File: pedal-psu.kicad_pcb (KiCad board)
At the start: 2 copper layers, 101.6 x 101.6 mm, 65 parts, among them J1 Conn_01x01_Male, J2 Conn_01x01_Male, J3 Conn_01x02_Male, J4 Conn_01x02_Male, J5 Conn_01x02_Male, J6 Conn_01x02_Male, T1 Transformer_1P_1S, T2 Transformer_1P_1S, U1 LM7809_TO220, U2 LM324, U4 LM7805_TO220, U5 LM317_3PinPackage

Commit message: Complete schematic, moving on to PCB design.
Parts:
- removed J5, J6: Conn_01x02_Male, Connector_Molex:Molex_KK-254_AE-6410-02A_1x02_P2.54mm_Vertical
- added C15: 100n, Capacitor_SMD:C_1210_3225Metric_Pad1.42x2.65mm_HandSolder, F.Cu at (266.8, 91.8)
- added C16: CP, Capacitor_THT:C_Radial_D10.0mm_H12.5mm_P5.00mm, F.Cu at (233.9, 95.4)
- added C17: CP, Capacitor_THT:C_Radial_D6.3mm_H5.0mm_P2.50mm, F.Cu at (244.9, 108.7)
- added C18: CP, Capacitor_THT:C_Radial_D6.3mm_H5.0mm_P2.50mm, F.Cu at (254.9, 99.6)
- added C19: 100n, Capacitor_SMD:C_1210_3225Metric_Pad1.42x2.65mm_HandSolder, F.Cu at (253.0, 106.8)
- added C20: 100n, Capacitor_SMD:C_1210_3225Metric_Pad1.42x2.65mm_HandSolder, F.Cu at (263.1, 96.3)
- added D10: 1N4001, Diode_SMD:D_SMA_Handsoldering, F.Cu at (247.2, 97.9)
- added D11: 1N4001, Diode_SMD:D_SMA_Handsoldering, F.Cu at (258.8, 91.9)
- added D12: 1N4001, Diode_SMD:D_SMA_Handsoldering, F.Cu at (247.2, 102.5)
- added D9: 1N4001, Diode_SMD:D_SMA_Handsoldering, F.Cu at (235.7, 109.5)
- added J7: Status LEDS, Connector_Molex:Molex_KK-254_AE-6410-10A_1x10_P2.54mm_Vertical, F.Cu at (306.1, 163.8)
- added R26: 220, Resistor_SMD:R_0805_2012Metric_Pad1.15x1.40mm_HandSolder, F.Cu at (240.0, 66.0)
- added R30: 100k, Resistor_SMD:R_0805_2012Metric_Pad1.15x1.40mm_HandSolder, F.Cu at (275.6, 145.8)
- added R31: 560, Resistor_SMD:R_0805_2012Metric_Pad1.15x1.40mm_HandSolder, F.Cu at (299.5, 161.3)
- added R32: 560, Resistor_SMD:R_0805_2012Metric_Pad1.15x1.40mm_HandSolder, F.Cu at (299.5, 158.8)
- added R33: 560, Resistor_SMD:R_0805_2012Metric_Pad1.15x1.40mm_HandSolder, F.Cu at (299.5, 156.2)
- added R34: 560, Resistor_SMD:R_0805_2012Metric_Pad1.15x1.40mm_HandSolder, F.Cu at (299.5, 153.7)
- added R35: 560, Resistor_SMD:R_0805_2012Metric_Pad1.15x1.40mm_HandSolder, F.Cu at (299.5, 151.1)
- added R36: 560, Resistor_SMD:R_0805_2012Metric_Pad1.15x1.40mm_HandSolder, F.Cu at (299.5, 148.6)
- added R37: 560, Resistor_SMD:R_0805_2012Metric_Pad1.15x1.40mm_HandSolder, F.Cu at (299.5, 146.1)
- added R38: 560, Resistor_SMD:R_0805_2012Metric_Pad1.15x1.40mm_HandSolder, F.Cu at (299.5, 143.5)
- added RV4: 10k, Potentiometer_THT:Potentiometer_Piher_PT-6-V_Vertical, F.Cu at (222.2, 57.1)
- added U3: LM7809_TO220, Package_TO_SOT_THT:TO-220-3_Vertical, F.Cu at (233.9, 105.1)
- added U6: LM7809_TO220, Package_TO_SOT_THT:TO-220-3_Vertical, F.Cu at (245.4, 93.6)
- added U7: 74HC595, Package_SO:SOP-16_4.4x10.4mm_P1.27mm, F.Cu at (288.9, 150.5)
- C12, D4, D6, R19, R25: moved to B.Cu
- J3: value Conn_01x02_Male -> Power Sockets; footprint Connector_Molex:Molex_KK-254_AE-6410-02A_1x02_P2.54mm_Vertical -> Connector_Molex:Molex_KK-254_AE-6410-10A_1x10_P2.54mm_Vertical
- J4: value Conn_01x02_Male -> LCD Display; footprint Connector_Molex:Molex_KK-254_AE-6410-02A_1x02_P2.54mm_Vertical -> Connector_Molex:Molex_KK-254_AE-6410-10A_1x10_P2.54mm_Vertical
- T1, T2: footprint Transformer_THT:Transformer_CHK_EI42-5VA_1xSec -> pedal-psu:Transformer_V42AJ
- moved A1 117.3 mm to (182.9, 158.8)
- moved R19 111.7 mm to (106.7, 142.2)
- moved C9 96.1 mm to (102.8, 109.2), turned to 180 degrees
- moved J3 94.6 mm to (121.9, 172.7)
- moved F2 87.8 mm to (113.0, 54.6)
- moved R25 86.8 mm to (104.1, 148.6), turned to 270 degrees
- moved RV2 85.3 mm to (105.4, 55.9), turned to 180 degrees
- moved D1 82.0 mm to (171.4, 99.1), turned to 180 degrees
- moved F1 80.0 mm to (161.3, 54.6)
- moved RV1 79.9 mm to (153.7, 55.9), turned to 180 degrees
- moved C14 68.3 mm to (100.3, 125.7)
- moved D6 66.6 mm to (97.8, 130.8), turned to 180 degrees
- moved D4 62.9 mm to (102.8, 135.9), turned to 180 degrees
- moved C12 60.1 mm to (96.5, 147.3)
- moved RV3 50.6 mm to (95.2, 142.2)
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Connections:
- net Net-(A1-Pad15) renamed MISO
- A1 pad 10: Net-(A1-Pad10) -> LCD7
- A1 pad 11: Net-(A1-Pad11) -> RS
- A1 pad 12: Net-(A1-Pad12) -> ENABLE
- A1 pad 13: Net-(A1-Pad13) -> SS
- A1 pad 14: Net-(A1-Pad14) -> MOSI
- A1 pad 16: Net-(A1-Pad16) -> SCK
- A1 pad 5: Net-(A1-Pad5) -> BUTTON
- A1 pad 7: Net-(A1-Pad7) -> LCD4
- A1 pad 8: Net-(A1-Pad8) -> LCD5
- A1 pad 9: Net-(A1-Pad9) -> LCD6
- C10 pad 2: Net-(C10-Pad2) -> GND
- C11 pad 2: Net-(C11-Pad2) -> GND
- C12 pad 2: Net-(C10-Pad2) -> GND
- C13 pad 2: Net-(C11-Pad2) -> GND
- C14 pad 2: Net-(C10-Pad2) -> GND
- C3 pad 1: +9V -> +9V_1
- C4 pad 1: +9V -> +9V_1
- C9 pad 2: Net-(C10-Pad2) -> GND
- D5 pad 2: +9V -> +9V_1
- D7 pad 1: +9V -> +9V_1
- D8 pad 2: Net-(C11-Pad2) -> GND
- J3 pad 1: +9V -> GND
- J3 pad 2: Net-(J3-Pad2) -> +9V_1
- J4 pad 1: +9V -> GND
- J4 pad 2: Net-(J4-Pad2) -> +5V
- R1 pad 1: +9V -> +9V_1
- R21 pad 1: Net-(J6-Pad2) -> GND_ADJ
- R3 pad 1: +9V -> +9V_2
- R5 pad 1: +9V -> +9V_3
- R7 pad 1: Net-(J3-Pad2) -> GND_1
- R8 pad 1: Net-(J4-Pad2) -> GND_2
- R9 pad 1: Net-(J5-Pad2) -> GND_3
- RV3 pad 2: Net-(C10-Pad2) -> GND
- RV3 pad 3: Net-(C10-Pad2) -> GND
- U1 pad 3: +9V -> +9V_1
- U2 pad 10: Net-(J5-Pad2) -> GND_3
- U2 pad 12: Net-(J6-Pad2) -> GND_ADJ
- U2 pad 3: Net-(J3-Pad2) -> GND_1
- U2 pad 5: Net-(J4-Pad2) -> GND_2
- U4 pad 2: Net-(C11-Pad2) -> GND
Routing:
- net Net-(J2-Pad1): track 0.00 -> 140.1 mm
- net Net-(F1-Pad2): track 0.00 -> 69.8 mm
- net Net-(F1-Pad1): track 0.00 -> 27.0 mm
- net Net-(F2-Pad1): track 0.00 -> 26.4 mm
- net Net-(C10-Pad1): track 0.00 -> 22.1 mm
- net Net-(C12-Pad1): track 0.00 -> 18.6 mm
- net Net-(R31-Pad1): track 0.00 -> 15.9 mm
- net +ADJV: track 0.00 -> 10.2 mm
- net Net-(R38-Pad1): track 0.00 -> 7.98 mm
- net Net-(R32-Pad1): track 0.00 -> 7.97 mm
- net Net-(R33-Pad1): track 0.00 -> 7.45 mm
- net Net-(R37-Pad1): track 0.00 -> 7.45 mm
- net Net-(R34-Pad1): track 0.00 -> 6.93 mm
- net Net-(R36-Pad1): track 0.00 -> 6.93 mm
- net Net-(R35-Pad1): track 0.00 -> 6.40 mm
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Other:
- board size 101.6 x 101.6 mm -> 139.7 x 101.6 mm
- net class Default: clearance 0.2 -> 0.4; trace_width 0.25 -> 0.6; via_dia 0.8 -> 1; via_drill 0.4 -> 0.5
- rule trace_clearance: 0.2 -> 0.4

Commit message: Moved things around on PCB
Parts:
- C19, C20, C4, D10, D11, D12, D5, D7, D9: moved to B.Cu
- moved C13 158.1 mm to (299.1, 35.8)
- moved J4 158.1 mm to (284.5, 62.2)
- moved R10 158.1 mm to (317.0, 23.1)
- moved R24 158.1 mm to (317.0, 20.2)
- moved R6 158.1 mm to (321.7, 18.6)
- moved A1 158.1 mm to (306.1, 59.7)
- moved C5 158.1 mm to (311.6, 23.0)
- moved C7 158.1 mm to (302.6, 30.9)
- moved C8 158.1 mm to (285.4, 43.6)
- moved R11 158.1 mm to (298.5, 39.3)
- moved R12 158.1 mm to (304.4, 34.5)
- moved R13 158.1 mm to (296.7, 43.0)
- moved R15 158.1 mm to (316.7, 17.2)
- moved R17 158.1 mm to (323.9, 15.6)
- moved R23 158.1 mm to (307.9, 30.2)
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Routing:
- net Net-(F2-Pad1): track 26.4 -> 27.0 mm
- net Net-(F1-Pad1): track 27.0 -> 26.4 mm

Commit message: Moving Op-Amp into place.
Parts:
- added C21: 100n, Capacitor_SMD:C_1210_3225Metric_Pad1.42x2.65mm_HandSolder, B.Cu at (163.4, 120.1)
- C12: value C -> 100n
- C13: value C -> 100n; moved to B.Cu
- C6, D3, D8, R20, R21, R7, R8, R9: moved to B.Cu
- D1, D2: footprint Diode_THT:Diode_Bridge_Vishay_KBL -> PartsStash:Diode_Bridge_TELPOD_GB009_p4mm
- F1, F2: footprint pedal-psu:Fuse-PTF15 -> PartsStash:Fuse-PTF15
- J1, J2: footprint pedal-psu:Blade_3866B.68 -> PartsStash:Blade_3866B.68
- T1, T2: footprint pedal-psu:Transformer_V42AJ -> PartsStash:Transformer_V42AJ
- U1, U3, U4, U5, U6: footprint Package_TO_SOT_THT:TO-220-3_Vertical -> PartsStash:TO220_Vertical_Radiator_L15mm_W10mm
- moved R17 233.2 mm to (121.4, 131.3), turned to 180 degrees
- moved R10 228.6 mm to (114.3, 128.8)
- moved R8 220.1 mm to (108.5, 137.0), turned to 90 degrees
- moved R7 208.5 mm to (103.4, 137.0), turned to 90 degrees
- moved R13 204.5 mm to (112.3, 131.3)
- moved R11 203.2 mm to (117.3, 131.3), turned to 180 degrees
- moved R21 192.8 mm to (118.6, 137.0), turned to 90 degrees
- moved R14 179.9 mm to (119.4, 128.8), turned to 180 degrees
- moved C8 176.2 mm to (163.4, 170.7), turned to 180 degrees
- moved C13 144.5 mm to (181.6, 119.9), turned to 180 degrees
- moved R16 134.5 mm to (110.2, 128.8)
- moved U2 108.2 mm to (115.8, 137.9), turned to 270 degrees
- moved R15 105.7 mm to (237.5, 87.1)
- moved R23 101.6 mm to (240.0, 105.8)
- moved R24 101.6 mm to (249.0, 95.8)
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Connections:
- T1 pad 3: Net-(D1-Pad3) -> Net-(D1-Pad2)
- T1 pad 4: Net-(D1-Pad2) -> Net-(D1-Pad3)
- U2 pad 1: Net-(R13-Pad1) -> Net-(R14-Pad1)
- U2 pad 2: Net-(R10-Pad1) -> Net-(R11-Pad1)
- U2 pad 3: GND_1 -> GND_2
- U2 pad 5: GND_2 -> GND_1
- U2 pad 6: Net-(R11-Pad1) -> Net-(R10-Pad1)
- U2 pad 7: Net-(R14-Pad1) -> Net-(R13-Pad1)
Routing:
- net Net-(C1-Pad1): track 0.00 -> 87.7 mm
- net +9V_3: track 0.00 -> 79.0 mm
- net +ADJV: track 10.2 -> 84.2 mm
- net +9V_2: track 0.00 -> 67.0 mm
- net Net-(C10-Pad1): track 22.1 -> 80.4 mm
- net +9V_1: track 0.00 -> 57.2 mm
- net Net-(D2-Pad3): track 0.00 -> 33.5 mm
- net Net-(D1-Pad3): track 0.00 -> 32.2 mm
- net +5V: track 0.00 -> 32.0 mm
- net GND_1: track 0.00 -> 27.0 mm, vias 0 -> 1
- net GND_2: track 0.00 -> 26.4 mm, vias 0 -> 1
- net Net-(D2-Pad2): track 0.00 -> 21.8 mm
- net Net-(D1-Pad2): track 0.00 -> 20.5 mm
- net GND_3: track 0.00 -> 14.9 mm, vias 0 -> 1
- net GND_ADJ: track 0.00 -> 14.6 mm, vias 0 -> 1
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
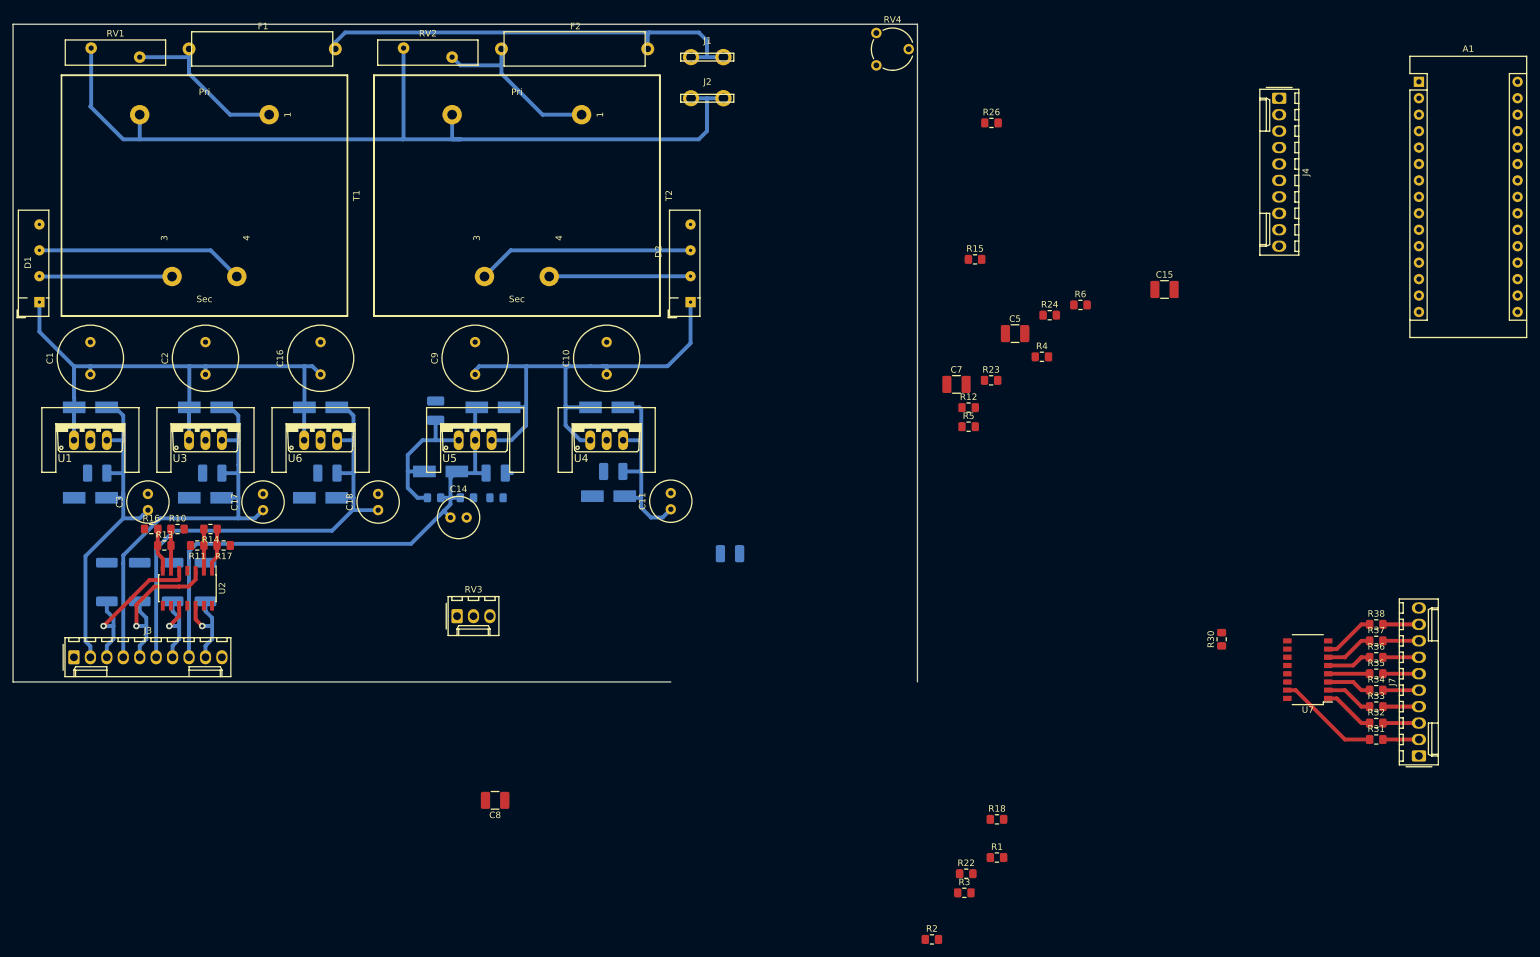
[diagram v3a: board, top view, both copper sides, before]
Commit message: Complete PCB ready for hand etching.
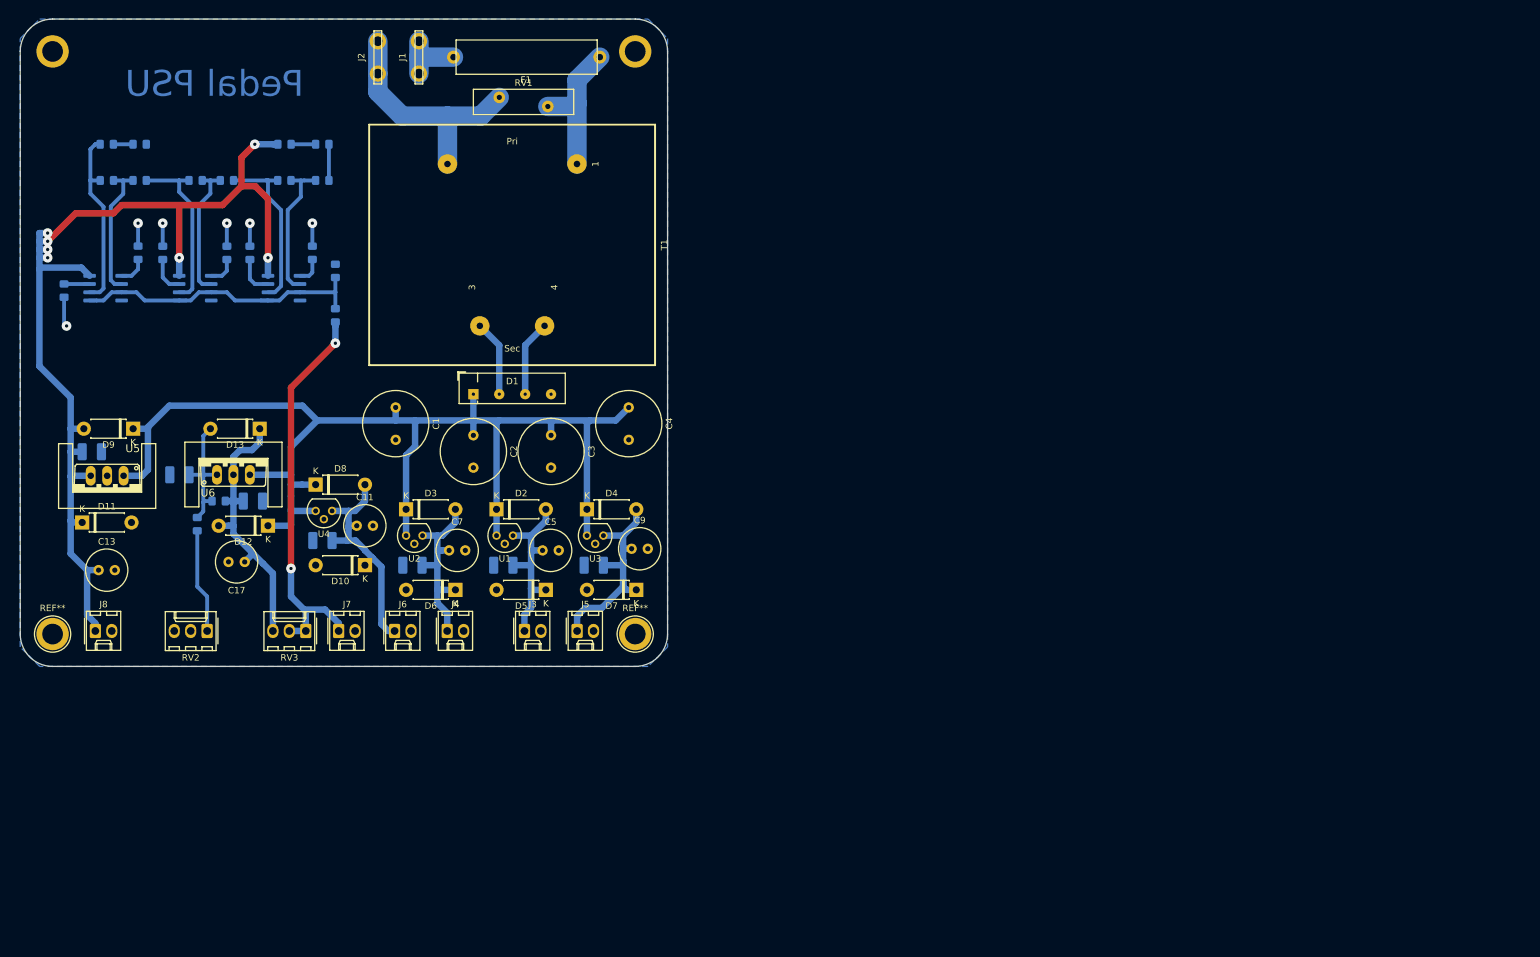
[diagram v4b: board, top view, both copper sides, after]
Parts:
- removed A1: Arduino_Nano_v3.x, Module:Arduino_Nano
- removed C18: CP, Capacitor_THT:C_Radial_D6.3mm_H5.0mm_P2.50mm
- removed C19, C20, C21: 100n, Capacitor_SMD:C_1210_3225Metric_Pad1.42x2.65mm_HandSolder
- removed F2: Fuse, PartsStash:Fuse-PTF15
- removed R21: R1, Resistor_SMD:R_2512_6332Metric_Pad1.52x3.35mm_HandSolder
- removed R22, R24: 1k, Resistor_SMD:R_0805_2012Metric_Pad1.15x1.40mm_HandSolder
- removed R23: 20k, Resistor_SMD:R_0805_2012Metric_Pad1.15x1.40mm_HandSolder
- removed R25: R, Resistor_SMD:R_0805_2012Metric_Pad1.15x1.40mm_HandSolder
- removed R26: 220, Resistor_SMD:R_0805_2012Metric_Pad1.15x1.40mm_HandSolder
- removed R30: 100k, Resistor_SMD:R_0805_2012Metric_Pad1.15x1.40mm_HandSolder
- removed R31, R32, R33, R34, R35, R36, R37, R38: 560, Resistor_SMD:R_0805_2012Metric_Pad1.15x1.40mm_HandSolder
- removed RV4: 10k, Potentiometer_THT:Potentiometer_Piher_PT-6-V_Vertical
- removed T2: Transformer_1P_1S, PartsStash:Transformer_V42AJ
- added ?: , , F.Cu at (0.00, -90.0)
- added ?: , , F.Cu at (-90.0, -90.0)
- added D13: 1N4001, Diode_THT:D_DO-41_SOD81_P7.62mm_Horizontal, F.Cu at (127.0, 113.3)
- added J5: Conn_01x02_Male, Connector_Molex:Molex_KK-254_AE-6410-02A_1x02_P2.54mm_Vertical, F.Cu at (176.0, 144.5)
- added J6: Conn_01x02_Male, Connector_Molex:Molex_KK-254_AE-6410-02A_1x02_P2.54mm_Vertical, F.Cu at (147.8, 144.5)
- added J8: Conn_01x02_Male, Connector_Molex:Molex_KK-254_AE-6410-02A_1x02_P2.54mm_Vertical, F.Cu at (101.6, 144.5)
- added REF**: Banana_Jack_1Pin, Connector:Banana_Jack_1Pin, F.Cu at (95.0, 145.0)
- added REF**: Banana_Jack_1Pin, Connector:Banana_Jack_1Pin, F.Cu at (185.0, 145.0)
- added U8: LM358, Package_SO:SOIC-8_3.9x4.9mm_P1.27mm, B.Cu at (117.0, 91.6)
- added U9: LM358, Package_SO:SOIC-8_3.9x4.9mm_P1.27mm, B.Cu at (130.7, 91.6)
- C10, C16: value CP -> 100n; footprint Capacitor_THT:C_Radial_D10.0mm_H12.5mm_P5.00mm -> Capacitor_SMD:C_1210_3225Metric_Pad1.42x2.65mm_HandSolder; moved to B.Cu
- C13: value 100n -> CP; footprint Capacitor_SMD:C_1210_3225Metric_Pad1.42x2.65mm_HandSolder -> Capacitor_THT:C_Radial_D6.3mm_H5.0mm_P2.50mm; moved to F.Cu
- C14: value CP -> 100n; footprint Capacitor_THT:C_Radial_D6.3mm_H5.0mm_P2.50mm -> Capacitor_SMD:C_1210_3225Metric_Pad1.42x2.65mm_HandSolder; moved to B.Cu
- C15, C8, R10, R11, R12: moved to B.Cu
- C3: footprint Capacitor_THT:C_Radial_D6.3mm_H5.0mm_P2.50mm -> Capacitor_THT:C_Radial_D10.0mm_H12.5mm_P5.00mm
- C4: value 100n -> CP; footprint Capacitor_SMD:C_1210_3225Metric_Pad1.42x2.65mm_HandSolder -> Capacitor_THT:C_Radial_D10.0mm_H12.5mm_P5.00mm; moved to F.Cu
- C5, C7: value 100n -> CP; footprint Capacitor_SMD:C_1210_3225Metric_Pad1.42x2.65mm_HandSolder -> Capacitor_THT:C_Radial_D6.3mm_H5.0mm_P2.50mm
- C9: footprint Capacitor_THT:C_Radial_D10.0mm_H12.5mm_P5.00mm -> Capacitor_THT:C_Radial_D6.3mm_H5.0mm_P2.50mm
- D10, D11, D12, D3, D4, D5, D6, D7, D8, D9: footprint Diode_SMD:D_SMA_Handsoldering -> Diode_THT:D_DO-41_SOD81_P7.62mm_Horizontal; moved to F.Cu
- D2: value D_Bridge_+AA- -> 1N4001; footprint PartsStash:Diode_Bridge_TELPOD_GB009_p4mm -> Diode_THT:D_DO-41_SOD81_P7.62mm_Horizontal
- J3: value Power Sockets -> Conn_01x02_Male; footprint Connector_Molex:Molex_KK-254_AE-6410-10A_1x10_P2.54mm_Vertical -> Connector_Molex:Molex_KK-254_AE-6410-02A_1x02_P2.54mm_Vertical
- J4: value LCD Display -> Conn_01x02_Male; footprint Connector_Molex:Molex_KK-254_AE-6410-10A_1x10_P2.54mm_Vertical -> Connector_Molex:Molex_KK-254_AE-6410-02A_1x02_P2.54mm_Vertical
- J7: value Status LEDS -> Conn_01x02_Male; footprint Connector_Molex:Molex_KK-254_AE-6410-10A_1x10_P2.54mm_Vertical -> Connector_Molex:Molex_KK-254_AE-6410-02A_1x02_P2.54mm_Vertical
- R1: value 10k -> 270; moved to B.Cu
- R13: value 20k -> 3k9; moved to B.Cu
- R14: value 20k -> 100R; moved to B.Cu
- R15: value 20k -> 470R; moved to B.Cu
- R16, R17, R18: value 1k -> 470R; moved to B.Cu
- R19: value 10k -> 470R
- R2: value 2k2 -> 470; moved to B.Cu
- R20: value 2k2 -> 470R
- R3: value 10k -> 22k; moved to B.Cu
- R4: value 2k2 -> 22k; moved to B.Cu
- R5: value 10k -> 3k9; moved to B.Cu
- R6: value 2k2 -> 3k9; moved to B.Cu
- R7: value R1 -> 1k2; footprint Resistor_SMD:R_2512_6332Metric_Pad1.52x3.35mm_HandSolder -> Resistor_SMD:R_0805_2012Metric_Pad1.15x1.40mm_HandSolder
- R8, R9: value R1 -> 1k; footprint Resistor_SMD:R_2512_6332Metric_Pad1.52x3.35mm_HandSolder -> Resistor_SMD:R_0805_2012Metric_Pad1.15x1.40mm_HandSolder
- RV2: value Varistor -> 1K; footprint Varistor:RV_Disc_D15.5mm_W3.9mm_P7.5mm -> Connector_Molex:Molex_KK-254_AE-6410-03A_1x03_P2.54mm_Vertical
- RV3: value 100k -> 2K
- U1, U3: value LM7809_TO220 -> LM78L09; footprint PartsStash:TO220_Vertical_Radiator_L15mm_W10mm -> Package_TO_SOT_THT:TO-92
- U2: value LM324 -> LM78L09; footprint Package_SO:SOIC-14_3.9x8.7mm_P1.27mm -> Package_TO_SOT_THT:TO-92
- U4: value LM7805_TO220 -> LM78L09; footprint PartsStash:TO220_Vertical_Radiator_L15mm_W10mm -> Package_TO_SOT_THT:TO-92
- U5: value LM317_3PinPackage -> LM7809_TO220
- U6: value LM7809_TO220 -> LM317_3PinPackage
- U7: value 74HC595 -> LM358; footprint Package_SO:SOP-16_4.4x10.4mm_P1.27mm -> Package_SO:SOIC-8_3.9x4.9mm_P1.27mm; moved to B.Cu
- moved U7 194.8 mm to (103.2, 91.6)
- moved J7 168.0 mm to (139.2, 144.5), turned to 0 degrees
- moved C15 154.8 mm to (114.6, 120.4), turned to 180 degrees
- moved J4 152.6 mm to (156.0, 144.5), turned to 0 degrees
- moved R18 147.7 mm to (121.9, 86.1), turned to 90 degrees
- moved R12 137.7 mm to (103.4, 74.9), turned to 180 degrees
- moved R1 132.2 mm to (120.7, 124.5), turned to 180 degrees
- moved R3 131.9 mm to (138.7, 95.8), turned to 90 degrees
- moved R2 130.4 mm to (117.3, 128.0), turned to 270 degrees
- moved R6 119.7 mm to (136.7, 69.3)
- moved R5 114.3 mm to (130.8, 69.3)
- moved R15 112.0 mm to (125.5, 86.1), turned to 90 degrees
- moved R4 109.9 mm to (138.7, 88.9), turned to 90 degrees
- moved RV2 96.4 mm to (118.9, 144.5)
- moved D7 85.5 mm to (185.2, 138.2)
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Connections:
- net VS3 renamed Net-(R5-Pad2)
- C1 pad 1: Net-(C1-Pad1) -> +12V
- C10 pad 1: Net-(C10-Pad1) -> +9V_2
- C11 pad 1: +5V -> +9V_1
- C12 pad 1: Net-(C12-Pad1) -> +9V_1
- C13 pad 1: +5V -> +9V_5
- C14 pad 1: +ADJV -> +9V_5
- C15 pad 1: +5V -> Net-(C15-Pad1)
- C16 pad 1: Net-(C1-Pad1) -> /ADJ
- C17 pad 1: +9V_2 -> /ADJ
- C2 pad 1: Net-(C1-Pad1) -> +12V
- C3 pad 1: +9V_1 -> +12V
- C4 pad 1: +9V_1 -> +12V
- C5 pad 1: IS1 -> +9V_3
- C6 pad 1: IS2 -> +9V_3
- C7 pad 1: IS3 -> +9V_4
- C8 pad 1: IS4 -> +9V_4
- C9 pad 1: Net-(C10-Pad1) -> +9V_2
- D1 pad 1: Net-(C1-Pad1) -> +12V
- D10 pad 1: Net-(C1-Pad1) -> +9V_1
- D10 pad 2: +9V_3 -> GND
- D11 pad 1: +9V_2 -> +9V_5
- D12 pad 1: +9V_3 -> +12V
- D12 pad 2: GND -> /ADJ
- D2 pad 1: Net-(C10-Pad1) -> +12V
- D2 pad 2: Net-(D2-Pad2) -> +9V_3
- D3 pad 1: Net-(C10-Pad1) -> +12V
- D3 pad 2: +5V -> +9V_4
- D4 pad 1: Net-(C10-Pad1) -> +12V
- D4 pad 2: +ADJV -> +9V_2
- D5 pad 1: Net-(C1-Pad1) -> +9V_3
- D5 pad 2: +9V_1 -> GND
- D6 pad 1: +ADJV -> +9V_4
- D6 pad 2: Net-(C12-Pad1) -> GND
- D7 pad 1: +9V_1 -> +9V_2
- D8 pad 1: +5V -> +12V
- D8 pad 2: GND -> +9V_1
- D9 pad 1: Net-(C1-Pad1) -> +12V
- D9 pad 2: +9V_2 -> +9V_5
- J3 pad 1: GND -> +9V_3
- J3 pad 2: +9V_1 -> GND
- J4 pad 1: GND -> +9V_4
- J4 pad 2: +5V -> GND
- J7 pad 1: GND -> +ADJV
- J7 pad 2: Net-(J7-Pad2) -> GND
- R1 pad 1: +9V_1 -> /ADJ
- R1 pad 2: VS1 -> Net-(C15-Pad1)
- R10 pad 2: GND -> Net-(R10-Pad2)
- R11 pad 1: Net-(R11-Pad1) -> Net-(R10-Pad2)
- R11 pad 2: GND -> Net-(R11-Pad2)
- R12 pad 1: Net-(R12-Pad1) -> Net-(R11-Pad2)
- R12 pad 2: GND -> Net-(R12-Pad2)
- R13 pad 1: Net-(R13-Pad1) -> Net-(R12-Pad2)
- R13 pad 2: Net-(R10-Pad1) -> Net-(R13-Pad2)
- R14 pad 1: Net-(R14-Pad1) -> Net-(R13-Pad2)
- R14 pad 2: Net-(R11-Pad1) -> GND
- R15 pad 2: Net-(R12-Pad1) -> Net-(R15-Pad2)
- R16 pad 1: IS1 -> Net-(R16-Pad1)
- R16 pad 2: Net-(R13-Pad1) -> Net-(R16-Pad2)
- R17 pad 1: IS2 -> Net-(R17-Pad1)
- R17 pad 2: Net-(R14-Pad1) -> Net-(R17-Pad2)
- R18 pad 1: IS3 -> Net-(R18-Pad1)
- R18 pad 2: Net-(R15-Pad1) -> Net-(R18-Pad2)
- R19 pad 1: +ADJV -> Net-(R19-Pad1)
- R19 pad 2: VS4 -> Net-(R19-Pad2)
- R2 pad 1: VS1 -> Net-(C15-Pad1)
- R2 pad 2: GND -> Net-(R2-Pad2)
- R20 pad 1: VS4 -> Net-(R20-Pad1)
- R20 pad 2: GND -> Net-(R20-Pad2)
- R3 pad 1: +9V_2 -> +ADJV
- R3 pad 2: VS2 -> V_SENSE
- R4 pad 1: VS2 -> V_SENSE
- R5 pad 1: +9V_3 -> +9V_5
- R6 pad 2: GND -> Net-(R6-Pad2)
- R7 pad 1: GND_1 -> Net-(R6-Pad2)
- R7 pad 2: GND -> Net-(R7-Pad2)
- R8 pad 1: GND_2 -> Net-(R7-Pad2)
- R8 pad 2: GND -> Net-(R8-Pad2)
- R9 pad 1: GND_3 -> Net-(R8-Pad2)
- R9 pad 2: GND -> Net-(R10-Pad1)
- RV2 pad 1: Net-(F2-Pad1) -> Net-(R2-Pad2)
- RV2 pad 2: Net-(J2-Pad1) -> GND
- RV3 pad 1: Net-(C12-Pad1) -> +ADJV
- RV3 pad 2: GND -> +ADJV
- RV3 pad 3: GND -> /ADJ
- U1 pad 1: Net-(C1-Pad1) -> +9V_3
- U1 pad 3: +9V_1 -> +12V
- U2 pad 1: Net-(R14-Pad1) -> +9V_4
- U2 pad 2: Net-(R11-Pad1) -> GND
- U2 pad 3: GND_2 -> +12V
- U3 pad 1: Net-(C1-Pad1) -> +9V_2
- U3 pad 3: +9V_2 -> +12V
- U4 pad 1: Net-(C10-Pad1) -> +9V_1
- U4 pad 3: +5V -> +12V
- U5 pad 1: Net-(C12-Pad1) -> +12V
- U5 pad 2: +ADJV -> GND
- U5 pad 3: Net-(C10-Pad1) -> +9V_5
- U6 pad 1: Net-(C1-Pad1) -> Net-(C15-Pad1)
- U6 pad 2: GND -> /ADJ
- U6 pad 3: +9V_3 -> +12V
- U7 pad 1: Net-(R32-Pad1) -> Net-(R20-Pad1)
- U7 pad 2: Net-(R33-Pad1) -> Net-(R11-Pad2)
- U7 pad 3: Net-(R34-Pad1) -> V_SENSE
- U7 pad 4: Net-(R35-Pad1) -> GND
- U7 pad 5: Net-(R36-Pad1) -> V_SENSE
- U7 pad 6: Net-(R37-Pad1) -> Net-(R12-Pad2)
- U7 pad 7: Net-(R38-Pad1) -> Net-(R19-Pad1)
- U7 pad 8: GND -> +9V_5
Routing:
- net +12V: track 0.00 -> 190.9 mm
- net +9V_5: track 0.00 -> 161.2 mm, vias 0 -> 7
- net Net-(J2-Pad1): track 140.1 -> 36.7 mm
- net Net-(C1-Pad1): track 87.7 -> 0.00 mm
- net Net-(C10-Pad1): track 80.4 -> 0.00 mm
- net Net-(F1-Pad2): track 69.8 -> 10.3 mm
- net +9V_3: track 79.0 -> 30.1 mm
- net V_SENSE: track 0.00 -> 45.4 mm
- net /ADJ: track 0.00 -> 43.4 mm
- net Net-(D2-Pad3): track 33.5 -> 0.00 mm
- net +5V: track 32.0 -> 0.00 mm
- net +9V_2: track 67.0 -> 35.3 mm
- net +9V_4: track 0.00 -> 30.3 mm
- net Net-(R12-Pad2): track 0.00 -> 28.1 mm
- net GND_1: track 27.0 -> 0.00 mm, vias 1 -> 0
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- added copper zone on B.Cu, net GND
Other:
- board size 139.7 x 101.6 mm -> 100 x 100 mm
- net class Default: via_dia 1 -> 1.5
- net class HighVoltage added: clearance 0.4, trace_width 3, via_dia 1.5, via_drill 0.5
- net class Power added: clearance 0.4, trace_width 1, via_dia 1.5, via_drill 0.5
- board text added: "Pedal PSU"
